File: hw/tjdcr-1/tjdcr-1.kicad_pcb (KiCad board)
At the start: 2 copper layers, 100.2 x 35 mm, 32 parts, among them J1 Conn_Coaxial, J2 Tuning Inductor, J3 Power, J4 LO Option, Q1 MMBT3904, Q2 MMBFJ310, T1 5:28, T2 28:5, T3 Transformer_1P_2S, T4 Transformer_1P_2S

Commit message: Layout is progressing
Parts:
- added C11: 0.1u, Capacitor_SMD:C_0805_2012Metric_Pad1.18x1.45mm_HandSolder, F.Cu at (78.0, 68.2)
- added C12: 47u, Capacitor_SMD:C_0805_2012Metric_Pad1.18x1.45mm_HandSolder, F.Cu at (86.2, 64.0)
- added C13: 470u (Size 2917/7343), Capacitor_Tantalum_SMD:CP_EIA-7343-20_Kemet-V_Pad2.25x2.55mm_HandSolder, F.Cu at (80.8, 77.5)
- added C14: 47u, Capacitor_SMD:C_0805_2012Metric_Pad1.18x1.45mm_HandSolder, F.Cu at (88.8, 68.2)
- added C15: 10u, Capacitor_SMD:C_0805_2012Metric_Pad1.18x1.45mm_HandSolder, F.Cu at (94.0, 68.2)
- added C16: 470u (Size 2917/7343), Capacitor_Tantalum_SMD:CP_EIA-7343-20_Kemet-V_Pad2.25x2.55mm_HandSolder, F.Cu at (96.8, 77.5)
- added C17: 10u, Capacitor_SMD:C_0805_2012Metric_Pad1.18x1.45mm_HandSolder, F.Cu at (106.0, 68.2)
- added C18: 470u (Size 2917/7343), Capacitor_Tantalum_SMD:CP_EIA-7343-20_Kemet-V_Pad2.25x2.55mm_HandSolder, F.Cu at (108.8, 77.5)
- added C19: 47u, Capacitor_SMD:C_0805_2012Metric_Pad1.18x1.45mm_HandSolder, F.Cu at (115.0, 68.2)
- added H1: MountingHole, MountingHole:MountingHole_2.5mm, F.Cu at (77.0, 54.0)
- added H2: MountingHole, MountingHole:MountingHole_2.5mm, F.Cu at (77.0, 83.0)
- added H3: MountingHole, MountingHole:MountingHole_2.5mm, F.Cu at (171.0, 54.0)
- added H4: MountingHole, MountingHole:MountingHole_2.5mm, F.Cu at (171.0, 83.0)
- added J5: Volume, Connector_PinHeader_2.54mm:PinHeader_1x03_P2.54mm_Vertical, F.Cu at (86.0, 83.0)
- added J6: Speaker, Connector_PinHeader_2.54mm:PinHeader_1x02_P2.54mm_Vertical, F.Cu at (114.0, 83.0)
- added Q3: MMBT3904, Package_TO_SOT_SMD:SOT-23, F.Cu at (82.3, 67.3)
- added Q4: MMBT3904, Package_TO_SOT_SMD:SOT-23, F.Cu at (98.5, 67.2)
- added Q5: 2N3904, Package_TO_SOT_THT:TO-92_Inline, F.Cu at (111.3, 68.2)
- added R10: 4.7k, Resistor_SMD:R_0805_2012Metric_Pad1.20x1.40mm_HandSolder, F.Cu at (78.0, 73.2)
- added R11: 470, Resistor_SMD:R_0805_2012Metric_Pad1.20x1.40mm_HandSolder, F.Cu at (83.0, 72.8)
- added R12: 220, Resistor_SMD:R_0805_2012Metric_Pad1.20x1.40mm_HandSolder, F.Cu at (88.8, 70.8)
- added R13: 4.7k, Resistor_SMD:R_0805_2012Metric_Pad1.20x1.40mm_HandSolder, F.Cu at (94.0, 73.2)
- added R14: 14.7k, Resistor_SMD:R_0805_2012Metric_Pad1.20x1.40mm_HandSolder, F.Cu at (94.0, 70.8)
- added R15: 1k, Resistor_SMD:R_0805_2012Metric_Pad1.20x1.40mm_HandSolder, F.Cu at (101.5, 67.2)
- added R16: 14.7k, Resistor_SMD:R_0805_2012Metric_Pad1.20x1.40mm_HandSolder, F.Cu at (106.0, 70.8)
- added R17: 470, Resistor_SMD:R_0805_2012Metric_Pad1.20x1.40mm_HandSolder, F.Cu at (97.8, 72.8)
- added R18: 4.7k, Resistor_SMD:R_0805_2012Metric_Pad1.20x1.40mm_HandSolder, F.Cu at (106.0, 73.2)
- added R20: 10, Resistor_SMD:R_0805_2012Metric_Pad1.20x1.40mm_HandSolder, F.Cu at (111.2, 72.8)
- added R8: 14.7k, Resistor_SMD:R_0805_2012Metric_Pad1.20x1.40mm_HandSolder, F.Cu at (78.0, 70.8)
- added R9: 1k, Resistor_SMD:R_0805_2012Metric_Pad1.20x1.40mm_HandSolder, F.Cu at (85.2, 67.2)
- added T5: Transformer_1P_1S, bruce-footprints:CheapAudioTransformer, F.Cu at (125.2, 73.8)
- added TP1: TestPoint, TestPoint:TestPoint_Pad_1.5x1.5mm, F.Cu at (146.0, 60.0)
- added TP2: TestPoint, TestPoint:TestPoint_Pad_1.5x1.5mm, F.Cu at (165.0, 55.0)
- added TP3: TestPoint, TestPoint:TestPoint_Pad_1.5x1.5mm, F.Cu at (101.8, 72.0)
- added TP4: TestPoint, TestPoint:TestPoint_Pad_1.5x1.5mm, F.Cu at (115.0, 73.0)
- J1: footprint Connector_Coaxial:SMA_Amphenol_901-143_Horizontal -> Connector_Coaxial:SMA_Amphenol_901-144_Vertical
- J2: value Tuning Inductor -> Tuning
- moved J3 31.9 mm to (104.5, 83.0)
- moved J4 21.7 mm to (146.5, 64.0)
- moved C10 5.30 mm to (167.0, 76.2)
- moved C5 5.30 mm to (140.8, 72.4)
- moved C6 5.30 mm to (138.2, 72.5)
- moved C7 5.30 mm to (143.2, 72.4)
- moved C8 5.30 mm to (155.8, 72.5)
- moved C9 5.30 mm to (153.2, 76.5)
- moved D3 5.30 mm to (159.2, 72.5)
- moved J2 5.30 mm to (143.0, 78.2)
- moved L2 5.30 mm to (165.0, 72.2)
- moved Q1 5.30 mm to (151.8, 72.4)
- moved Q2 5.30 mm to (163.4, 76.5)
- moved R2 5.30 mm to (145.8, 72.5)
- moved R3 5.30 mm to (148.2, 72.5)
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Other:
- board size 100.2 x 35 mm -> 100 x 35 mm

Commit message: All wires connected
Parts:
- moved J3 4.54 mm to (100.0, 82.2)
- moved J2 4.00 mm to (139.2, 76.8)
- moved C10 1.40 mm to (167.0, 74.8)
- moved C6 1.40 mm to (138.2, 71.1)
- moved C8 1.40 mm to (155.8, 71.1)
- moved C9 1.40 mm to (153.2, 75.1)
- moved D3 1.40 mm to (159.2, 71.1)
- moved Q2 1.40 mm to (163.4, 75.1)
- moved R2 1.40 mm to (145.8, 71.1)
- moved R3 1.40 mm to (148.2, 71.1)
- moved R4 1.40 mm to (150.8, 75.1)
- moved R5 1.40 mm to (155.8, 75.1)
- moved R6 1.40 mm to (160.0, 75.1), turned to 90 degrees
- moved R7 1.40 mm to (162.5, 70.8)
- moved C5 1.40 mm to (140.8, 71.0)
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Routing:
- net Audio: track 0.00 -> 104.2 mm
- net GND: track 0.00 -> 40.2 mm, vias 0 -> 20
- net LO_O: track 0.00 -> 31.3 mm
- net Net-(J2-Pin_1): track 0.00 -> 26.6 mm
- net Net-(Q5-C): track 0.00 -> 21.9 mm
- net Net-(D1-K): track 0.00 -> 19.5 mm
- net Net-(D3-K): track 0.00 -> 18.3 mm
- net +9V: track 0.00 -> 17.1 mm, vias 0 -> 8
- net Net-(J5-Pin_2): track 0.00 -> 15.9 mm
- net Net-(J5-Pin_1): track 0.00 -> 15.5 mm
- net Net-(T4-SB): track 0.00 -> 14.9 mm
- net Net-(D2-COM): track 0.00 -> 12.8 mm
- net Net-(Q2-G): track 0.00 -> 11.6 mm
- net Net-(Q4-C): track 0.00 -> 11.4 mm
- net Net-(Q5-B): track 0.00 -> 11.2 mm
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- added copper zone on In2.Cu, net +9V
- added copper zone on In1.Cu, net GND
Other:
- copper layers 2 -> 4
- board text added: "(No Si5351!)"
- board text added: "9V"
- board text added: "AF Out"
- board text added: "ANT"
- board text added: "G"
- board text added: "Gain"
- board text added: "KC1FSZ bruce@mackinnon.com"
- board text added: "LO Option"
- board text added: "Power"
- board text added: "SPK"
- board text added: "T"
- board text added: "TJ DRC 2025-02"
- board text added: "Tune"
- board text added: "W"

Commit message: Working
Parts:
- added C20: 0.47u, Capacitor_SMD:C_0805_2012Metric_Pad1.18x1.45mm_HandSolder, F.Cu at (166.8, 58.5)
- moved C10 0.65 mm to (167.0, 75.5)
- moved C6 0.65 mm to (138.2, 71.8)
- moved C8 0.65 mm to (155.8, 71.7)
- moved C9 0.65 mm to (153.2, 75.7)
- moved D3 0.65 mm to (159.2, 71.7)
- moved J2 0.65 mm to (139.2, 77.5)
- moved Q2 0.65 mm to (163.4, 75.7)
- moved R2 0.65 mm to (145.8, 71.7)
- moved R3 0.65 mm to (148.2, 71.7)
- moved R4 0.65 mm to (150.8, 75.7)
- moved R5 0.65 mm to (155.8, 75.7)
- moved R6 0.65 mm to (160.0, 75.7)
- moved R7 0.65 mm to (162.5, 71.5)
- moved C5 0.65 mm to (140.8, 71.7)
- moved C7 0.65 mm to (143.2, 71.7)
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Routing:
- net GND: track 40.2 -> 37.0 mm, vias 20 -> 90
- net Audio: track 104.2 -> 107.0 mm
- added copper zone on F.Cu, net GND
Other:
- board text added: "Circuit Design by N2CQR and KK4DAS"
- board text added: "Ext"
- board text added: "PCB Design by KC1FSZ"
- board text added: "Thomas Jefferson Direct Conversion Receiver"

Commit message: Checkpoint before adding variable caps
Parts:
- added C21: 0.1u, Capacitor_SMD:C_0805_2012Metric_Pad1.18x1.45mm_HandSolder, F.Cu at (166.0, 78.5)
- C11: value 0.1u -> 0.33u
- C13, C16, C18: footprint Capacitor_Tantalum_SMD:CP_EIA-7343-20_Kemet-V_Pad2.25x2.55mm_HandSolder -> bruce-footprints:CP_EIA-7343
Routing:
- net Net-(Q2-S): track 2.96 -> 6.22 mm

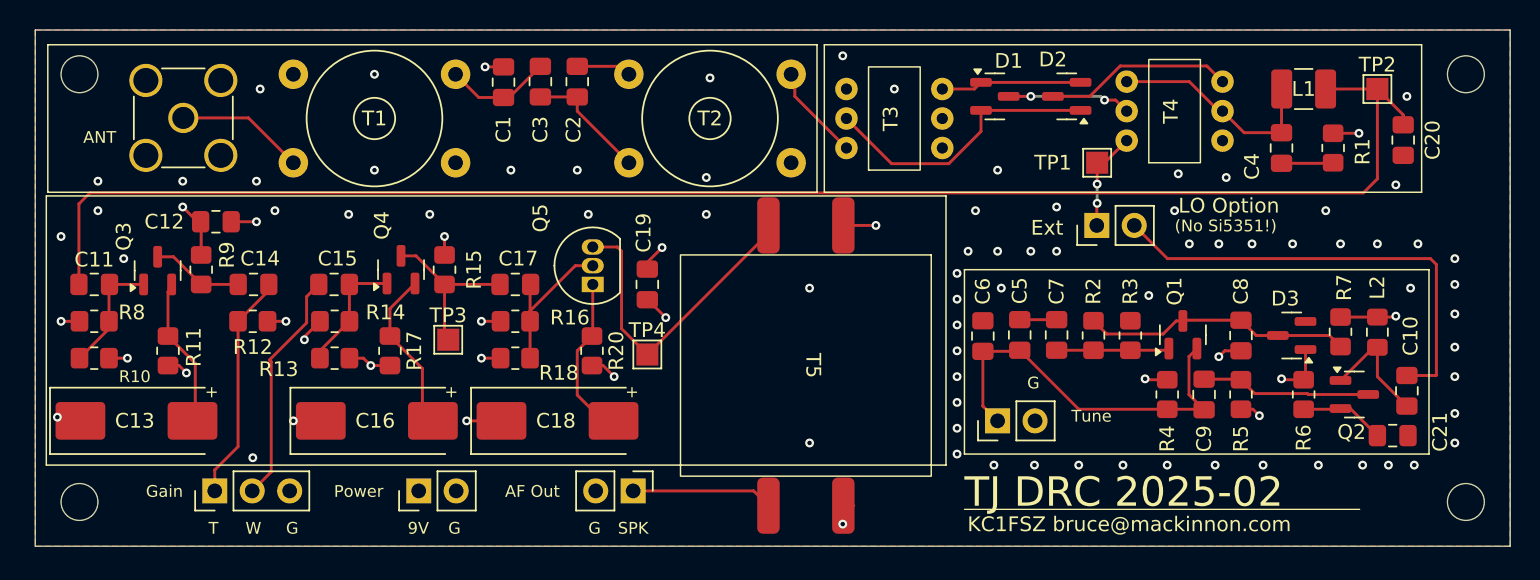
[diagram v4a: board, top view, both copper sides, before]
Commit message: Checkpoint after audio transformer change, preparing for flip of audio amp
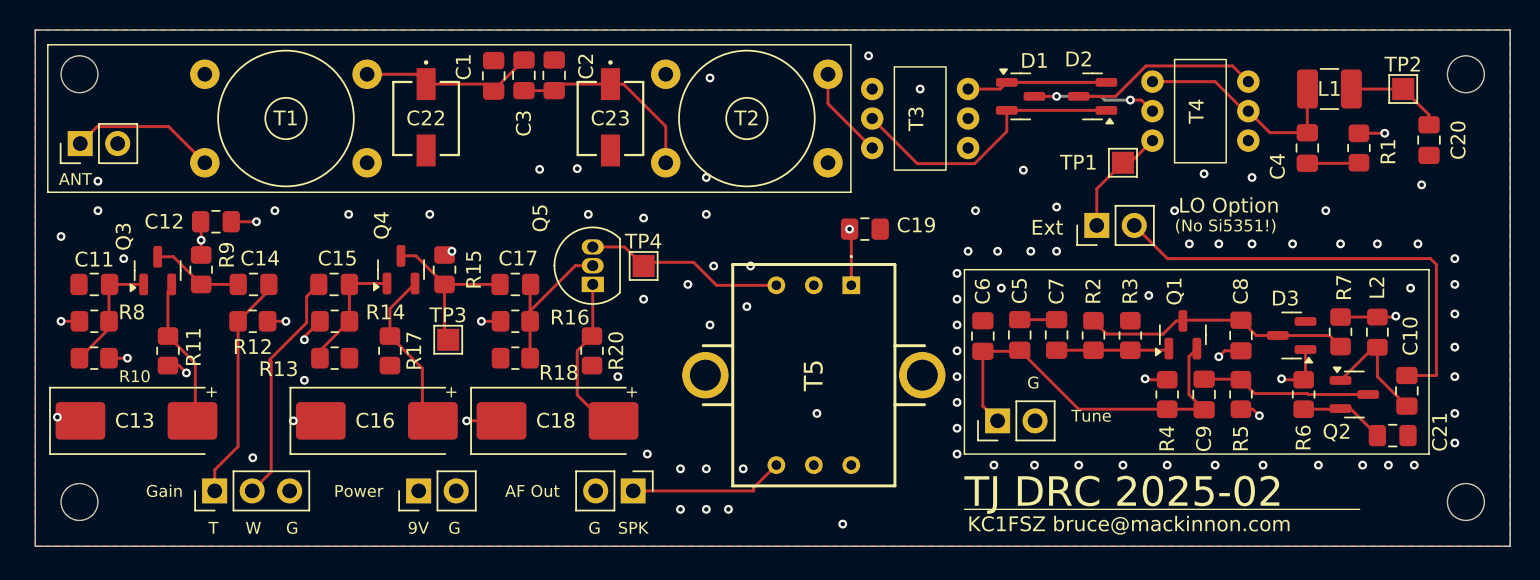
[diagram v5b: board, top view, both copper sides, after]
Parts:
- added C22: C_Variable, bruce-footprints:VCAP_GKG30086-05_SGM-L, F.Cu at (100.5, 57.0)
- added C23: C_Variable, bruce-footprints:VCAP_GKG30086-05_SGM-L, F.Cu at (113.0, 57.0)
- C11: value 0.33u -> 33u
- J1: footprint Connector_Coaxial:SMA_Amphenol_901-144_Vertical -> Connector_PinHeader_2.54mm:PinHeader_1x02_P2.54mm_Vertical
- R20: value 10 -> 100
- T5: value Transformer_1P_1S -> 42TL013-RC; footprint bruce-footprints:CheapAudioTransformer -> bruce-footprints:42TL013RC
- moved C19 15.2 mm to (130.2, 64.5), turned to 180 degrees
- moved J1 7.20 mm to (77.0, 58.7)
- moved T5 6.25 mm to (129.3, 68.3)
- moved TP4 6.01 mm to (115.2, 67.0)
- moved T1 6.00 mm to (85.5, 60.0)
- moved T2 2.50 mm to (127.8, 54.0)
- moved C20 1.75 mm to (168.5, 58.5)
- moved C4 1.75 mm to (160.2, 59.0)
- moved D1 1.75 mm to (140.8, 55.5)
- moved D2 1.75 mm to (145.7, 55.5)
- moved L1 1.75 mm to (161.8, 55.0)
- moved R1 1.75 mm to (163.8, 59.0)
- moved T3 1.75 mm to (133.8, 57.0)
- moved T4 1.75 mm to (152.8, 56.5)
- moved TP1 1.75 mm to (147.8, 60.0)
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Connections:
- T5 pad 2: Net-(Q5-C) -> unconnected-(T5-P2-Pad2)
- T5 pad 3: GND -> Net-(Q5-C)
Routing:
- net Audio: track 107.0 -> 6.66 mm
- net GND: track 37.0 -> 23.4 mm, vias 90 -> 94
- net Net-(Q5-C): track 21.9 -> 13.7 mm
- net Net-(T2-SB): track 8.41 -> 13.5 mm
- net Net-(T1-SB): track 7.28 -> 12.0 mm
- net +9V: track 17.1 -> 14.5 mm, vias 8 -> 7
- net Net-(J1-In): track 8.72 -> 9.94 mm
- net /Speaker Out: track 9.58 -> 10.6 mm
- net LO_I: track 6.88 -> 7.61 mm, vias 2 -> 0

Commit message: Checkpoint after audio amp reverse
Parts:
- added TP5: TestPoint, TestPoint:TestPoint_Pad_1.5x1.5mm, F.Cu at (131.5, 62.0)
- moved C11 55.2 mm to (132.7, 75.2), turned to 180 degrees
- moved R10 54.8 mm to (132.7, 70.2), turned to 180 degrees
- moved R8 54.7 mm to (132.7, 72.8), turned to 180 degrees
- moved C19 50.9 mm to (82.0, 80.8), turned to 0 degrees
- moved C13 50.5 mm to (130.0, 66.0), turned to 180 degrees
- moved T5 48.4 mm to (81.7, 76.9), turned to 90 degrees
- moved Q3 47.0 mm to (128.4, 76.2), turned to -90 degrees
- moved R11 44.8 mm to (127.7, 70.8), turned to 90 degrees
- moved C12 41.2 mm to (124.5, 79.5), turned to 0 degrees
- moved R9 41.2 mm to (125.5, 76.2), turned to 90 degrees
- moved C14 33.8 mm to (121.9, 75.2), turned to 0 degrees
- moved J5 33.4 mm to (119.5, 81.8), turned to -90 degrees
- moved R12 33.3 mm to (122.0, 72.8), turned to 180 degrees
- moved J6 28.3 mm to (86.2, 81.8), turned to 90 degrees
- moved C15 23.3 mm to (116.5, 75.2), turned to 0 degrees
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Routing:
- net Audio: track 6.66 -> 53.3 mm, vias 0 -> 2
- net GND: track 23.4 -> 11.4 mm, vias 94 -> 78
- net Net-(J5-Pin_2): track 16.0 -> 6.70 mm
- net /Speaker Out: track 10.6 -> 18.1 mm
- net LO_O: track 31.1 -> 23.7 mm
- net +9V: track 14.5 -> 9.00 mm
- net Net-(J5-Pin_1): track 15.5 -> 10.4 mm
- net Net-(J1-In): track 9.94 -> 6.29 mm
- net Net-(T2-AA): track 6.24 -> 9.55 mm
- net Net-(Q2-D): track 8.25 -> 5.96 mm
- net Net-(T1-SB): track 12.0 -> 13.2 mm
- net Net-(T2-SB): track 13.5 -> 14.5 mm
- net Net-(Q5-C): track 13.7 -> 13.1 mm

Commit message: Ready to send this version to fab
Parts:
- C1, C2: value 160p -> 150p
- moved T3 0.75 mm to (133.8, 56.2)
- moved TP5 0.75 mm to (131.5, 61.2)
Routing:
- net Net-(D1-K): track 19.5 -> 21.1 mm
- net Net-(T1-SB): track 13.2 -> 11.7 mm
- net Net-(T2-SB): track 14.5 -> 13.7 mm
- net Net-(T2-AA): track 9.55 -> 8.80 mm
- net GND: vias 78 -> 79

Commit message: Corrected schematic error
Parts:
- moved C6 2.52 mm to (141.8, 71.8)
- moved C5 2.48 mm to (139.2, 71.7)
- moved C7 0.27 mm to (144.5, 71.7)
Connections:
- C5 pad 1: Net-(C5-Pad1) -> Net-(J2-Pin_1)
- C5 pad 2: Net-(J2-Pin_1) -> Net-(Q1-E)
- C6 pad 1: Net-(J2-Pin_1) -> Net-(Q1-E)
- C7 pad 1: Net-(C5-Pad1) -> Net-(J2-Pin_1)
- C9 pad 1: Net-(J2-Pin_1) -> Net-(Q1-E)
- Q1 pad 2: Net-(J2-Pin_1) -> Net-(Q1-E)
- R4 pad 1: Net-(J2-Pin_1) -> Net-(Q1-E)
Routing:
- net Net-(Q1-E): track 0.00 -> 21.3 mm
- net Net-(J2-Pin_1): track 26.6 -> 17.1 mm
- net Net-(C5-Pad1): track 2.50 -> 0.00 mm
- net GND: vias 79 -> 80
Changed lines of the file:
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@@
 	(net 12 "Net-(T2-AA)")
 	(net 13 "Net-(J2-Pin_1)")
-	(net 14 "Net-(C5-Pad1)")
+	(net 14 "Net-(Q1-E)")
 	(net 15 "Net-(Q1-B)")
 	(net 16 "Net-(D3-K)")
@@
 			(layers "F.Cu" "F.Paste" "F.Mask")
 			(roundrect_rratio 0.25)
-			(net 13 "Net-(J2-Pin_1)")
+			(net 14 "Net-(Q1-E)")
 			(pinfunction "E")
 			(pintype "passive")
@@
 			(layers "F.Cu" "F.Paste" "F.Mask")
 			(roundrect_rratio 0.208333)
-			(net 13 "Net-(J2-Pin_1)")
+			(net 14 "Net-(Q1-E)")
 			(pintype "passive")
 		)
@@
 			(layers "F.Cu" "F.Paste" "F.Mask")
 			(roundrect_rratio 0.212766)
-			(net 13 "Net-(J2-Pin_1)")
+			(net 14 "Net-(Q1-E)")
 			(pintype "passive")
 		)
@@
 	(footprint "Capacitor_SMD:C_0805_2012Metric_Pad1.18x1.45mm_HandSolder"
 		(layer "F.Cu")
-		(at 139.23 71.75 90)
+		(at 141.75 71.75 90)
 		(descr "Capacitor SMD 0805 (2012 Metric), square (rectangular) end terminal, IPC_7351 nominal with elongated pad for handsoldering. (Body size source: IPC-SM-782 page 76, https://www.pcb-3d.com/wordpress/wp-content/uploads/ipc-sm-782a_amendment_1_and_2.pdf, https://docs.google.com/spreadsheets/d/1BsfQQcO9C6DZCsRaXUlFlo91Tg2WpOkGARC1WS5S8t0/edit?usp=sharing), generated with kicad-footprint-generator")
 		(tags "capacitor handsolder")
@@
 			(layers "F.Cu" "F.Paste" "F.Mask")
 			(roundrect_rratio 0.212766)
-			(net 13 "Net-(J2-Pin_1)")
+			(net 14 "Net-(Q1-E)")
 			(pintype "passive")
 		)
@@
 	(footprint "Capacitor_SMD:C_0805_2012Metric_Pad1.18x1.45mm_HandSolder"
 		(layer "F.Cu")
-		(at 141.73 71.675 -90)
+		(at 139.25 71.7125 -90)
 		(descr "Capacitor SMD 0805 (2012 Metric), square (rectangular) end terminal, IPC_7351 nominal with elongated pad for handsoldering. (Body size source: IPC-SM-782 page 76, https://www.pcb-3d.com/wordpress/wp-content/uploads/ipc-sm-782a_amendment_1_and_2.pdf, https://docs.google.com/spreadsheets/d/1BsfQQcO9C6DZCsRaXUlFlo91Tg2WpOkGARC1WS5S8t0/edit?usp=sharing), generated with kicad-footprint-generator")
 		(tags "capacitor handsolder")
@@
 			(layers "F.Cu" "F.Paste" "F.Mask")
 			(roundrect_rratio 0.212766)
-			(net 14 "Net-(C5-Pad1)")
+			(net 13 "Net-(J2-Pin_1)")
 			(pintype "passive")
 		)
@@
 			(layers "F.Cu" "F.Paste" "F.Mask")
 			(roundrect_rratio 0.212766)
-			(net 13 "Net-(J2-Pin_1)")
+			(net 14 "Net-(Q1-E)")
 			(pintype "passive")
 		)
@@
 	(footprint "Capacitor_SMD:C_0805_2012Metric_Pad1.18x1.45mm_HandSolder"
 		(layer "F.Cu")
-		(at 144.23 71.675 -90)
+		(at 144.5 71.675 -90)
 		(descr "Capacitor SMD 0805 (2012 Metric), square (rectangular) end terminal, IPC_7351 nominal with elongated pad for handsoldering. (Body size source: IPC-SM-782 page 76, https://www.pcb-3d.com/wordpress/wp-content/uploads/ipc-sm-782a_amendment_1_and_2.pdf, https://docs.google.com/spreadsheets/d/1BsfQQcO9C6DZCsRaXUlFlo91Tg2WpOkGARC1WS5S8t0/edit?usp=sharing), generated with kicad-footprint-generator")
 		(tags "capacitor handsolder")
@@
 			(layers "F.Cu" "F.Paste" "F.Mask")
 			(roundrect_rratio 0.212766)
-			(net 14 "Net-(C5-Pad1)")
+			(net 13 "Net-(J2-Pin_1)")
 			(pintype "passive")
 		)
@@
 	)
 	(segment
-		(start 139.23 70.7125)
-		(end 139.23 70.65)
-		(width 0.2)
-		(layer "F.Cu")
-		(net 1)
-	)
-	(segment
 		(start 161.105 72.6625)
 		(end 161.105 74.5875)
@@
 	)
 	(via
+		(at 140.5 69)
+		(size 0.6)
+		(drill 0.3)
+		(layers "F.Cu" "B.Cu")
+		(free yes)
+		(net 1)
+	)
+	(via
 		(at 167.75 65.5)
 		(size 0.6)
@@
 	)
 	(segment
-		(start 139.23 76.5)
-		(end 140.23 77.5)
+		(start 139.23 70.7125)
+		(end 139.23 70.65)
 		(width 0.2)
 		(layer "F.Cu")
@@
 	)
 	(segment
-		(start 139.23 72.7875)
-		(end 139.23 76.5)
+		(start 138.225 75.495)
+		(end 138.225 71.7)
 		(width 0.2)
 		(layer "F.Cu")
@@
 	)
 	(segment
-		(start 151.73 76.7125)
-		(end 154.1925 76.7125)
+		(start 142.75 68)
+		(end 144.23 69.48)
 		(width 0.2)
 		(layer "F.Cu")
@@
 	)
 	(segment
-		(start 153.7425 72.6)
-		(end 153.205 73.1375)
+		(start 138.225 71.7)
+		(end 139.25 70.675)
 		(width 0.2)
 		(layer "F.Cu")
@@
 	)
 	(segment
-		(start 139.23 72.7875)
-		(end 141.655 72.7875)
+		(start 144.23 69.48)
+		(end 144.23 70.6375)
 		(width 0.2)
 		(layer "F.Cu")
@@
 	)
 	(segment
-		(start 153.205 75.725)
-		(end 154.23 76.75)
+		(start 139.25 68.75)
+		(end 140 68)
 		(width 0.2)
 		(layer "F.Cu")
@@
 	)
 	(segment
-		(start 141.73 72.7125)
-		(end 145.73 76.7125)
+		(start 139.25 70.675)
+		(end 139.25 68.75)
 		(width 0.2)
 		(layer "F.Cu")
@@
 	)
 	(segment
-		(start 154.1925 76.7125)
-		(end 154.23 76.75)
+		(start 140.23 77.5)
+		(end 138.225 75.495)
 		(width 0.2)
 		(layer "F.Cu")
@@
 	)
 	(segment
-		(start 145.73 76.7125)
-		(end 151.73 76.7125)
+		(start 140 68)
+		(end 142.75 68)
 		(width 0.2)
 		(layer "F.Cu")
@@
 	)
 	(segment
+		(start 146 76.7125)
+		(end 151.73 76.7125)
+		(width 0.2)
+		(layer "F.Cu")
+		(net 14)
+	)
+	(segment
+		(start 151.73 76.7125)
+		(end 154.1925 76.7125)
+		(width 0.2)
+		(layer "F.Cu")
+		(net 14)
+	)
+	(segment
+		(start 139.25 72.75)
+		(end 139.5 72.75)
+		(width 0.2)
+		(layer "F.Cu")
+		(net 14)
+	)
+	(segment
+		(start 145.925 76.7125)
+		(end 146 76.7125)
+		(width 0.2)
+		(layer "F.Cu")
+		(net 14)
+	)
+	(segment
+		(start 142 72.7875)
+		(end 145.925 76.7125)
+		(width 0.2)
+		(layer "F.Cu")
+		(net 14)
+	)
+	(segment
+		(start 153.7425 72.6)
+		(end 153.205 73.1375)
+		(width 0.2)
+		(layer "F.Cu")
+		(net 14)
+	)
+	(segment
+		(start 153.205 75.725)
+		(end 154.23 76.75)
+		(width 0.2)
+		(layer "F.Cu")
+		(net 14)
+	)
+	(segment
+		(start 154.1925 76.7125)
+		(end 154.23 76.75)
+		(width 0.2)
+		(layer "F.Cu")
+		(net 14)
+	)
+	(segment
+		(start 139.5 72.75)
+		(end 139.5375 72.7875)
+		(width 0.2)
+		(layer "F.Cu")
+		(net 14)
+	)
+	(segment
+		(start 141.9625 72.75)
+		(end 142 72.7875)
+		(width 0.2)
+		(layer "F.Cu")
+		(net 14)
+	)
+	(segment
 		(start 141.655 72.7875)
 		(end 141.73 72.7125)
 		(width 0.2)
 		(layer "F.Cu")
-		(net 13)
+		(net 14)
 	)
 	(segment
-		(start 153.205 73.1375)
-		(end 153.205 75.725)
+		(start 139.5375 72.7875)
+		(end 141.75 72.7875)
 		(width 0.2)
 		(layer "F.Cu")
-		(net 13)
+		(net 14)
 	)
 	(segment
-		(start 141.73 70.6375)
-		(end 144.23 70.6375)
+		(start 153.205 73.1375)
+		(end 153.205 75.725)
 		(width 0.2)
 		(layer "F.Cu")
@@
 	)
 	(segment
-		(start 144.23 72.7125)
+		(start 144.5 72.7125)
 		(end 146.73 72.7125)
 		(width 0.2)
